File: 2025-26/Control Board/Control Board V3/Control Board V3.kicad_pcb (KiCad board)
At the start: 4 copper layers, 75 x 125 mm, 70 parts, among them J1 PM01, J10 J_5V, J11 UART, J2 CM01, J3 Mini PC, J4 Motor 1, J5 Motor 2, J6 Motor 3, J7 Motor 4, J8 Motor 0, J9 J_GND, Q2 CSD16301Q2, Q4 LMG5200, U1 ADS8684IDBTR, U2 INA240A2PWR, U3 ADS8684IDBTR, U4 INA240A2PWR, U5 TPS54308DDCR, U6 INA240A2PWR

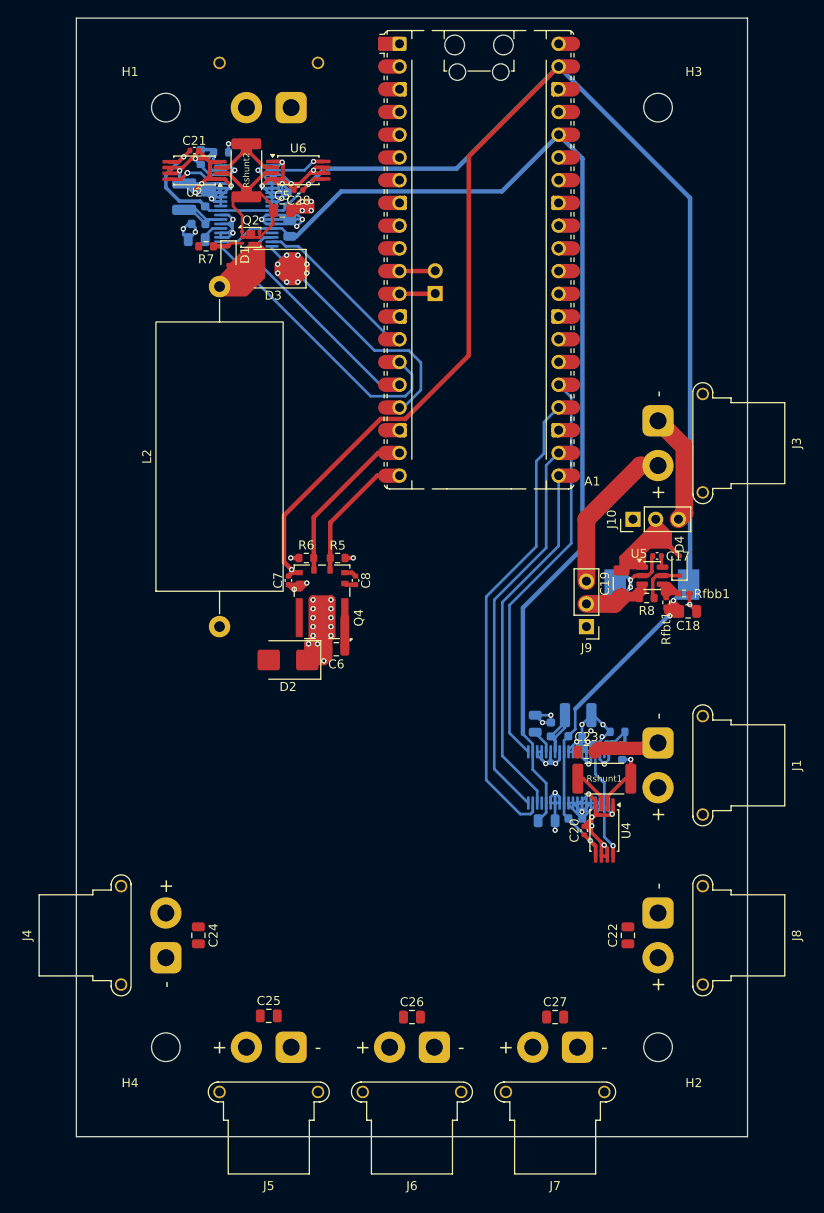
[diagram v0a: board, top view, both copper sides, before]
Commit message: so much..
so, not much change to pcbs, mainly the job files are now included.

on the controls side there is a vibe coded mess that needs to be cleaned up. making a checkpoint because i want to see if a separate claude chat can clean up the code first.
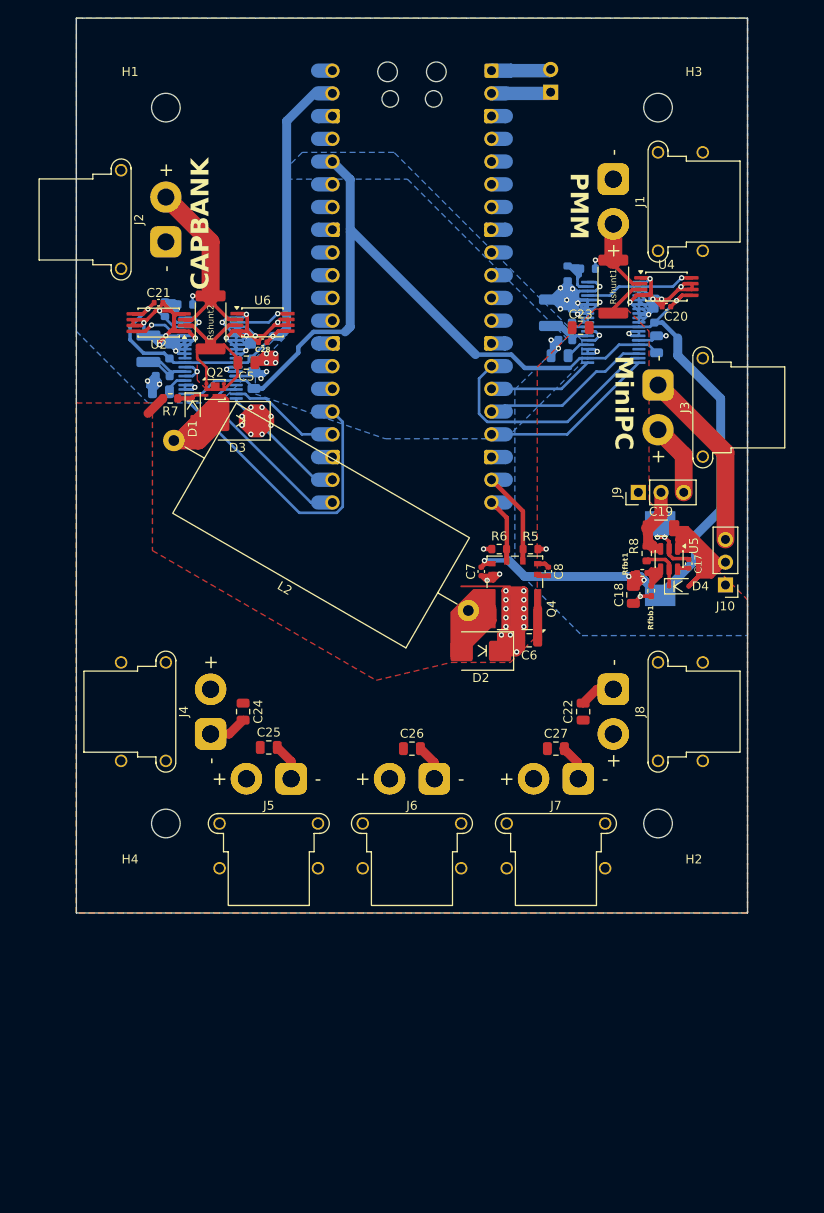
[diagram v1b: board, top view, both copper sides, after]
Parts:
- added J12: Motor 1, Connector_AMASS:AMASS_XT30PW-M_1x02_P2.50mm_Horizontal, B.Cu at (25.0, 90.0)
- added J13: Motor 2, Connector_AMASS:AMASS_XT30PW-M_1x02_P2.50mm_Horizontal, B.Cu at (34.0, 95.0)
- added J14: Motor 3, Connector_AMASS:AMASS_XT30PW-M_1x02_P2.50mm_Horizontal, B.Cu at (50.0, 95.0)
- added J15: Motor 4, Connector_AMASS:AMASS_XT30PW-M_1x02_P2.50mm_Horizontal, B.Cu at (66.1, 95.0)
- added J16: Motor 0, Connector_AMASS:AMASS_XT30PW-M_1x02_P2.50mm_Horizontal, B.Cu at (70.0, 85.0)
- added J17: PM01, Connector_AMASS:AMASS_XT30PW-M_1x02_P2.50mm_Horizontal, B.Cu at (70.0, 28.0)
- A1: moved to B.Cu
- J2: moved to F.Cu
- moved J1 63.2 mm to (70.0, 28.0)
- moved U4 61.2 mm to (75.9, 40.0), turned to 0 degrees
- moved C20 59.3 mm to (75.9, 42.2), turned to 0 degrees
- moved C1 56.9 mm to (74.6, 43.2), turned to 90 degrees
- moved Rshunt1 55.0 mm to (70.0, 40.0), turned to -90 degrees
- moved C2 54.6 mm to (74.8, 46.5), turned to 90 degrees
- moved R1 54.2 mm to (67.2, 38.0), turned to 180 degrees
- moved R2 51.5 mm to (64.9, 38.5), turned to -90 degrees
- moved U3 51.1 mm to (70.0, 44.0), turned to 0 degrees
- moved C23 47.4 mm to (66.3, 44.6), turned to 180 degrees
- moved C10 47.0 mm to (65.4, 43.2), turned to 90 degrees
- moved C9 45.1 mm to (63.0, 42.9), turned to 90 degrees
- moved C11 43.5 mm to (64.6, 46.0), turned to 180 degrees
- moved C12 41.2 mm to (64.0, 47.7), turned to 180 degrees
- moved C27 30.0 mm to (63.6, 91.6)
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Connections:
- A1 pad 1: unconnected-(A1-GPIO0-Pad1) -> Net-(A1-GPIO0)
- A1 pad 11: Net-(A1-GPIO8) -> unconnected-(A1-GPIO8-Pad11)
- A1 pad 12: Net-(A1-GPIO9) -> unconnected-(A1-GPIO9-Pad12)
- A1 pad 13: Net-(A1-GND-Pad13) -> DGND
- A1 pad 18: Net-(A1-GND-Pad13) -> DGND
- A1 pad 19: PWM_L -> PWM_H
- A1 pad 2: unconnected-(A1-GPIO1-Pad2) -> Net-(A1-GPIO1)
- A1 pad 20: PWM_H -> PWM_L
- A1 pad 23: Net-(A1-GND-Pad13) -> DGND
- A1 pad 28: Net-(A1-GND-Pad13) -> DGND
- A1 pad 3: Net-(A1-GND-Pad13) -> DGND
- A1 pad 33: unconnected-(A1-AGND-Pad33) -> DGND
- A1 pad 38: Net-(A1-GND-Pad13) -> DGND
- A1 pad 8: Net-(A1-GND-Pad13) -> DGND
- C1 pad 2: /Measurement System 1/PGND -> PGND
- C10 pad 2: /Measurement System 1/PGND -> PGND
- C11 pad 2: /Measurement System 1/PGND -> PGND
- C12 pad 2: /Measurement System 1/PGND -> PGND
- C13 pad 2: /Measurement System 2/PGND -> PGND
- C14 pad 2: /Measurement System 2/PGND -> PGND
- C15 pad 2: /Measurement System 2/PGND -> PGND
- C16 pad 2: /Measurement System 2/PGND -> PGND
- C20 pad 1: DGND -> PGND
- C21 pad 1: DGND -> PGND
- C28 pad 2: DGND -> PGND
- C3 pad 2: /Measurement System 2/PGND -> PGND
- C9 pad 2: /Measurement System 1/PGND -> PGND
- J11 pad 1: Net-(A1-GPIO9) -> Net-(A1-GPIO1)
- J11 pad 2: Net-(A1-GPIO8) -> Net-(A1-GPIO0)
- R2 pad 2: DGND -> PGND
- R4 pad 2: DGND -> PGND
- U1 pad 1: SPI1_MOSI -> SPI0_MOSI
- U1 pad 10: /Measurement System 2/PGND -> PGND
- U1 pad 11: /Measurement System 2/PGND -> PGND
- U1 pad 12: /Measurement System 2/PGND -> PGND
- U1 pad 13: /Measurement System 2/PGND -> PGND
- U1 pad 14: /Measurement System 2/PGND -> PGND
- U1 pad 15: /Measurement System 2/PGND -> PGND
- U1 pad 17: /Measurement System 2/PGND -> PGND
- U1 pad 19: /Measurement System 2/PGND -> PGND
- U1 pad 20: /Measurement System 2/PGND -> PGND
- U1 pad 22: /Measurement System 2/PGND -> PGND
- U1 pad 23: /Measurement System 2/PGND -> PGND
- U1 pad 24: /Measurement System 2/PGND -> PGND
- U1 pad 25: /Measurement System 2/PGND -> PGND
- U1 pad 26: /Measurement System 2/PGND -> PGND
- U1 pad 27: /Measurement System 2/PGND -> PGND
- U1 pad 28: /Measurement System 2/PGND -> PGND
- U1 pad 29: /Measurement System 2/PGND -> PGND
- U1 pad 31: /Measurement System 2/PGND -> PGND
- U1 pad 32: /Measurement System 2/PGND -> PGND
- U1 pad 36: SPI1_MISO -> SPI0_MISO
- U1 pad 37: SPI1_CLK -> SPI0_CLK
- U1 pad 38: SPI1_CS -> SPI0_CS
- U1 pad 6: /Measurement System 2/PGND -> PGND
- U1 pad 8: /Measurement System 2/PGND -> PGND
- U2 pad 1: DGND -> PGND
- U2 pad 4: DGND -> PGND
- U2 pad 6: DGND -> PGND
- U2 pad 7: DGND -> PGND
- U3 pad 1: SPI0_MOSI -> SPI1_MOSI
- U3 pad 10: /Measurement System 1/PGND -> PGND
- U3 pad 11: /Measurement System 1/PGND -> PGND
- U3 pad 12: /Measurement System 1/PGND -> PGND
- U3 pad 13: /Measurement System 1/PGND -> PGND
- U3 pad 14: /Measurement System 1/PGND -> PGND
- U3 pad 15: /Measurement System 1/PGND -> PGND
- U3 pad 17: /Measurement System 1/PGND -> PGND
- U3 pad 19: /Measurement System 1/PGND -> PGND
- U3 pad 20: /Measurement System 1/PGND -> PGND
- U3 pad 22: /Measurement System 1/PGND -> PGND
- U3 pad 23: /Measurement System 1/PGND -> PGND
- U3 pad 24: /Measurement System 1/PGND -> PGND
- U3 pad 25: /Measurement System 1/PGND -> PGND
- U3 pad 26: /Measurement System 1/PGND -> PGND
- U3 pad 27: /Measurement System 1/PGND -> PGND
- U3 pad 28: /Measurement System 1/PGND -> PGND
- U3 pad 29: /Measurement System 1/PGND -> PGND
- U3 pad 31: /Measurement System 1/PGND -> PGND
- U3 pad 32: /Measurement System 1/PGND -> PGND
- U3 pad 36: SPI0_MISO -> SPI1_MISO
- U3 pad 37: SPI0_CLK -> SPI1_CLK
- U3 pad 38: SPI0_CS -> SPI1_CS
- U3 pad 6: /Measurement System 1/PGND -> PGND
- U3 pad 8: /Measurement System 1/PGND -> PGND
- U4 pad 1: DGND -> PGND
- U4 pad 4: DGND -> PGND
- U4 pad 6: DGND -> PGND
- U4 pad 7: DGND -> PGND
- U6 pad 1: DGND -> PGND
- U6 pad 4: DGND -> PGND
- U6 pad 6: DGND -> PGND
- U6 pad 7: DGND -> PGND
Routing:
- net PGND: track 28.5 -> 257.2 mm, vias 25 -> 61
- net DGND: track 247.3 -> 27.0 mm, vias 42 -> 10
- net 5V: track 246.9 -> 145.1 mm
- net 3V3: track 125.4 -> 84.1 mm
- net SPI0_CLK: track 52.9 -> 12.6 mm
- net SPI0_CS: track 43.7 -> 13.9 mm
- net SPI1_MOSI: track 32.3 -> 11.2 mm
- net SPI0_MISO: track 40.8 -> 20.0 mm
- net CM01: track 15.4 -> 28.5 mm
- net SPI0_MOSI: track 45.3 -> 34.3 mm
- net PWM_L: track 18.5 -> 8.60 mm
- net SPI1_CS: track 28.5 -> 19.0 mm
- net MiniPC+: track 17.4 -> 8.19 mm
- net SPI1_CLK: track 18.8 -> 27.1 mm
- net MiniPC-: track 12.5 -> 20.4 mm
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- added copper zone on B.Cu, net 3V3
- added copper zone on B.Cu, net 5V
- added copper zone on B.Cu, net DGND
- added copper zone on In2.Cu, net DGND
- added copper zone on F.Cu, net PGND
- added copper zone on F.Cu, net V_DT
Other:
- board size 75 x 125 mm -> 75 x 100 mm
- board text added: "CAPBANK"
- board text added: "MiniPC"
- board text added: "PMM"
